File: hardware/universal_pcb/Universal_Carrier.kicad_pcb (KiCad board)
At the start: 2 copper layers, 100 x 70 mm, 98 parts

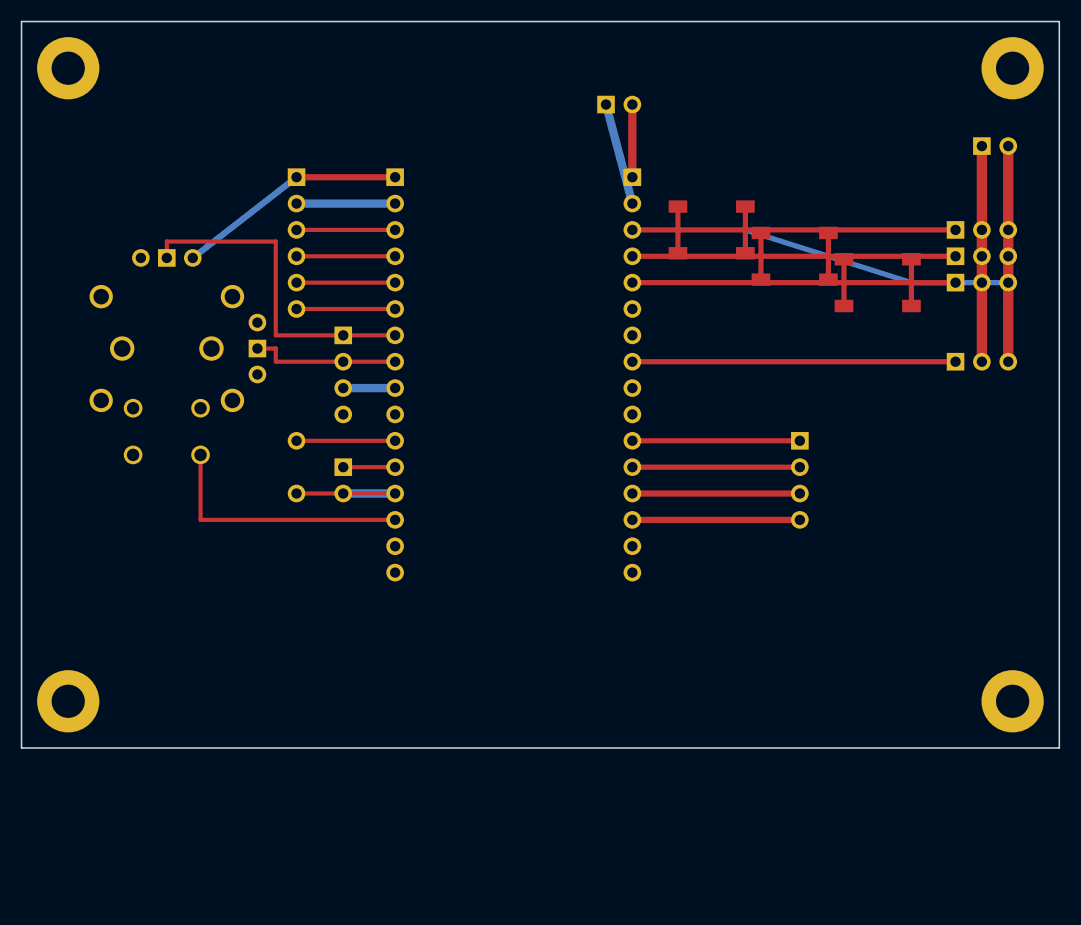
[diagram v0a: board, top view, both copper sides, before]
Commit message: chore: add local history tracking and lock files for universal pcb hardware project
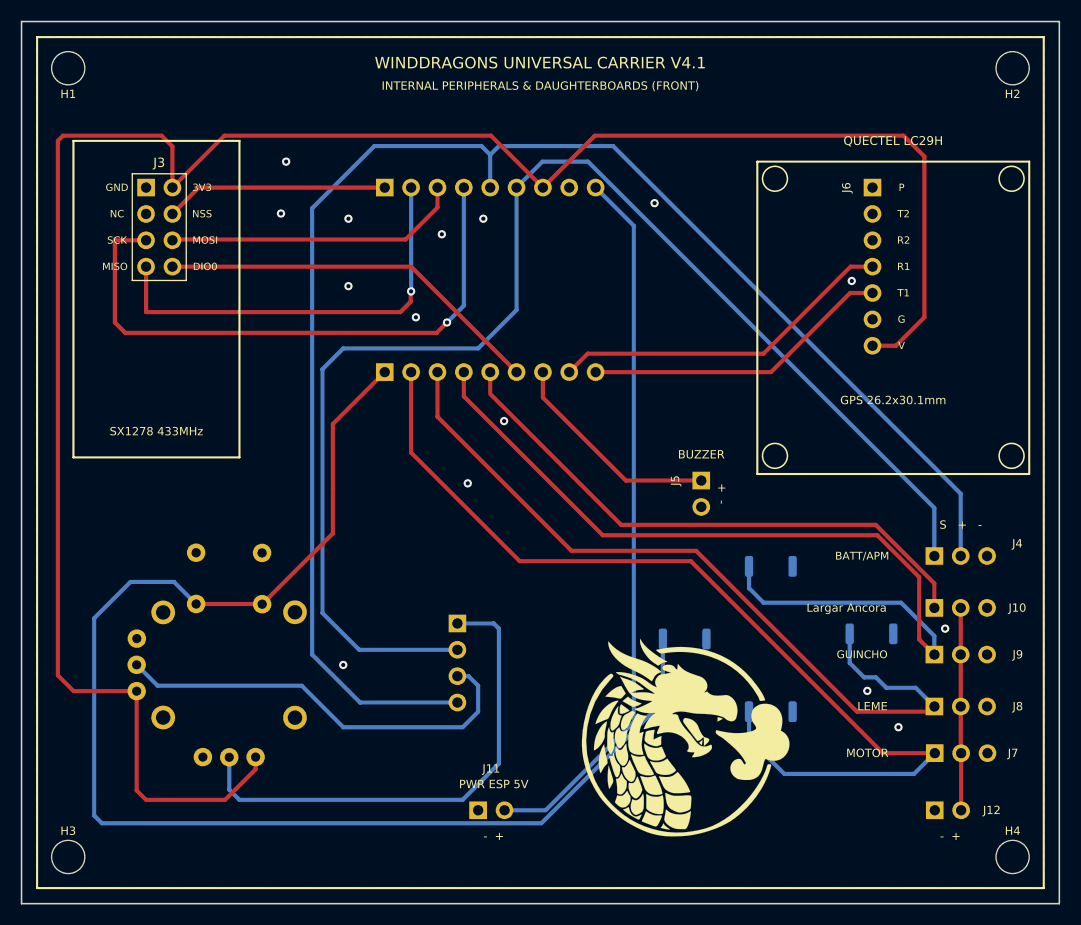
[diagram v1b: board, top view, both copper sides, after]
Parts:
- removed ? (x4): , MountingHole:MountingHole_3.2mm_M3_Pad
- removed ? (x82): , Connector_PinHeader_2.54mm:PinHeader_1x01_P2.54mm_Vertical
- removed ? (x12): , Button_Switch_SMD:SW_Push_1P1T_NO_6x6mm_H9.5mm
- added H1: MountingHole, MountingHole:MountingHole_3.2mm_M3, F.Cu at (4.50, 4.50)
- added H2: MountingHole, MountingHole:MountingHole_3.2mm_M3, F.Cu at (95.5, 4.50)
- added H3: MountingHole, MountingHole:MountingHole_3.2mm_M3, F.Cu at (4.50, 80.5)
- added H4: MountingHole, MountingHole:MountingHole_3.2mm_M3, F.Cu at (95.5, 80.5)
- added J1: ESP32_T_LANDSCAPE, Connector_PinHeader_2.54mm:PinHeader_1x09_P2.54mm_Horizontal, B.Cu at (35.0, 16.0)
- added J10: RACK_CREMALHEIRA, Connector_PinHeader_2.54mm:PinHeader_1x03_P2.54mm_Horizontal, F.Cu at (88.0, 56.5)
- added J11: PWR_ESP_5V, Connector_PinHeader_2.54mm:PinHeader_1x02_P2.54mm_Horizontal, F.Cu at (44.0, 76.0)
- added J12: PWR_SERVO_5V, Connector_PinHeader_2.54mm:PinHeader_1x02_P2.54mm_Horizontal, F.Cu at (88.0, 76.0)
- added J2: ESP32_B_LANDSCAPE, Connector_PinHeader_2.54mm:PinHeader_1x09_P2.54mm_Horizontal, B.Cu at (35.0, 33.8)
- added J3: SX1278_LORA_2x4, Connector_PinHeader_2.54mm:PinHeader_2x04_P2.54mm_Vertical, F.Cu at (12.0, 16.0)
- added J4: BATT_APM, Connector_PinHeader_2.54mm:PinHeader_1x03_P2.54mm_Horizontal, F.Cu at (88.0, 51.5)
- added J5: BUZZER, Connector_PinHeader_2.54mm:PinHeader_1x02_P2.54mm_Vertical, F.Cu at (65.5, 44.2)
- added J6: GPS_LC29H_7PIN, Connector_PinHeader_2.54mm:PinHeader_1x07_P2.54mm_Vertical, F.Cu at (82.0, 16.0)
- added J7: ESC_PROP_UP, Connector_PinHeader_2.54mm:PinHeader_1x03_P2.54mm_Horizontal, F.Cu at (88.0, 70.5)
- added J8: RUDDER_DN, Connector_PinHeader_2.54mm:PinHeader_1x03_P2.54mm_Horizontal, F.Cu at (88.0, 66.0)
- added J9: WINCH_MODE, Connector_PinHeader_2.54mm:PinHeader_1x03_P2.54mm_Horizontal, F.Cu at (88.0, 61.0)
- added JOY1: PS4_JOYSTICK, PS4_joystick:XDCR_COM-09032, B.Cu at (20.0, 62.0)
- added JP_RBL: REMOVE_BEFORE_LAUNCH, Connector_PinHeader_2.54mm:PinHeader_1x04_P2.54mm_Vertical, B.Cu at (42.0, 58.0)
- added LOGO1: WindDragons_Logo, WindDragons:WindDragons_Logo_20mm, F.Cu at (64.0, 69.0)
- added LOGO2: WindDragons_Logo, WindDragons:WindDragons_Logo_14mm, B.Cu at (50.5, 49.0)
- added SW1: UP, PS4_joystick:SKRKAEE020, B.Cu at (72.2, 66.5)
- added SW2: MODE, PS4_joystick:SKRKAEE020, B.Cu at (81.9, 59.0)
- added SW3: DOWN, PS4_joystick:SKRKAEE020, B.Cu at (72.2, 52.5)
- added SW4: BOOT, PS4_joystick:SKRKAEE020, B.Cu at (63.9, 59.5)
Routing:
- net 0: track 476.5 -> 0.00 mm
- net /+3V3: track 0.00 -> 200.3 mm
- net /IO1_ADC: track 0.00 -> 147.6 mm
- net /IO9_BOOT: track 0.00 -> 130.8 mm
- net /IO0_ADC: track 0.00 -> 130.6 mm
- net /IO18_ACT1_UP: track 0.00 -> 93.0 mm
- net /IO20_RUDDER_DN: track 0.00 -> 85.2 mm
- net /IO19_WINCH_MODE: track 0.00 -> 77.3 mm
- net /+5V: track 0.00 -> 69.0 mm
- net /IO2_SCK: track 0.00 -> 57.5 mm, vias 0 -> 1
- net /IO23_ACT4: track 0.00 -> 55.3 mm
- net /JOY_X: track 0.00 -> 48.2 mm
- net /JOY_Y: track 0.00 -> 41.6 mm
- net /IO4_MISO: track 0.00 -> 41.3 mm, vias 0 -> 1
- net /IO12_LORA_DIO0: track 0.00 -> 37.4 mm
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- added copper zone on B.Cu, net /GND
- added copper zone on F.Cu, net /GND
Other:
- board size 100 x 70 mm -> 100 x 85 mm
- rule pad_to_mask_clearance: 0.1 -> 0.05
- board text added: "+ -"
- board text added: "- +"
- board text added: "BATT/APM"
- board text added: "BUZZER"
- board text added: "GPS 26.2x30.1mm"
- board text added: "GUINCHO"
- board text added: "INTERNAL PERIPHERALS & DAUGHTERBOARDS (FRONT)"
- board text added: "LEME"
- board text added: "Largar Ancora"
- board text added: "MOTOR"
- board text added: "PS4 3D JOYSTICK"
- board text added: "PWR ESP 5V"
- board text added: "QUECTEL LC29H"
- board text added: "REMOVE BEFORE LAUNCH"
- board text added: "S + -"
- board text added: "SOLID GND COPPER PLANES ON F.CU & B.CU (100x85mm)"
- board text added: "ST7789 1.47 INCH LCD (320x172)"
- board text added: "SX1278 433MHz"
- board text added: "USB-C"
- board text added: "USER INTERFACE: DISPLAY & PS4 JOYSTICK"
- board text added: "WINDDRAGONS REMOTE CONTROL & CARRIER V4.1"
- board text added: "WINDDRAGONS UNIVERSAL CARRIER V4.1"
- board text added: "X: 1-2 | Y: 3-4"

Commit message: feat: add new universal PCB gerbers, logos, and updated design files
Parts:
- moved LOGO1 4.12 mm to (60.0, 68.0)
- moved LOGO2 1.00 mm to (50.5, 48.0)

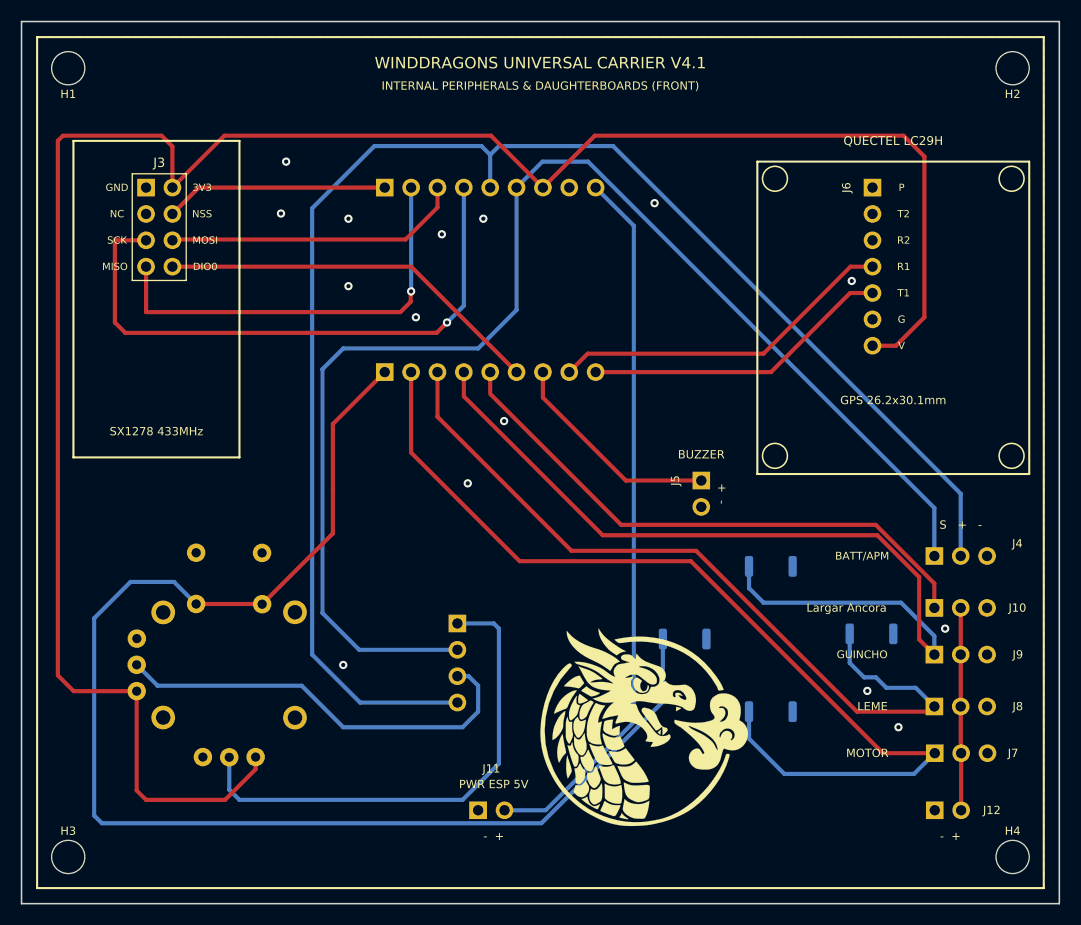
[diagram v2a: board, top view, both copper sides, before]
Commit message: feat: update PCB gerber files and add logo bitmap header
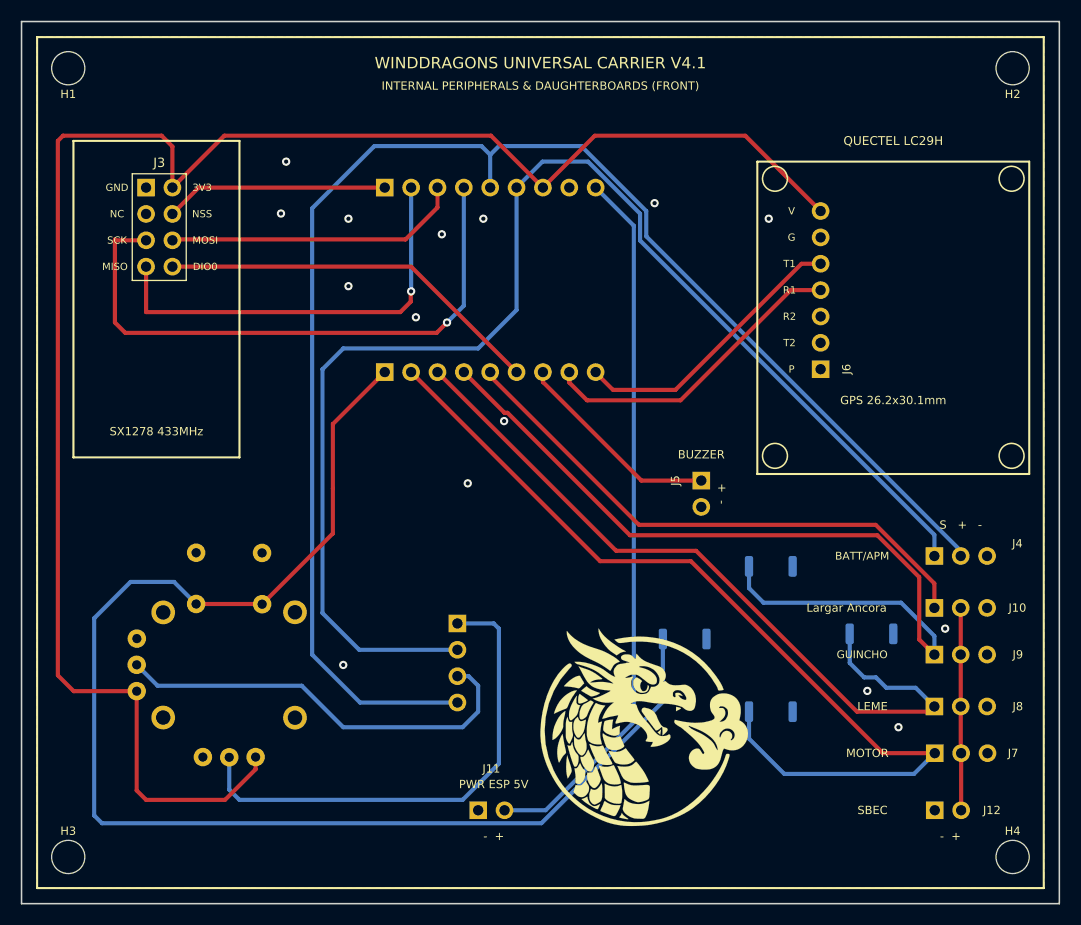
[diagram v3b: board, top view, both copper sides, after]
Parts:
- moved J6 18.2 mm to (77.0, 33.5), turned to 180 degrees
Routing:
- net /+3V3: track 200.3 -> 170.8 mm
- net /IO18_ACT1_UP: track 93.0 -> 88.5 mm
- net /IO16_GPS_RX: track 33.4 -> 30.3 mm
- net /IO19_WINCH_MODE: track 77.3 -> 74.8 mm
- net /IO17_GPS_TX: track 29.8 -> 27.5 mm
- net /IO1_ADC: track 147.6 -> 145.8 mm
- net /IO20_RUDDER_DN: track 85.2 -> 83.8 mm
- net /IO13_BUZ: track 21.0 -> 20.2 mm
- net /IO23_ACT4: track 55.3 -> 54.5 mm
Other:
- board text added: "SBEC"

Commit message: feat: add web configuration page and API endpoints for screen brightness control and system settings
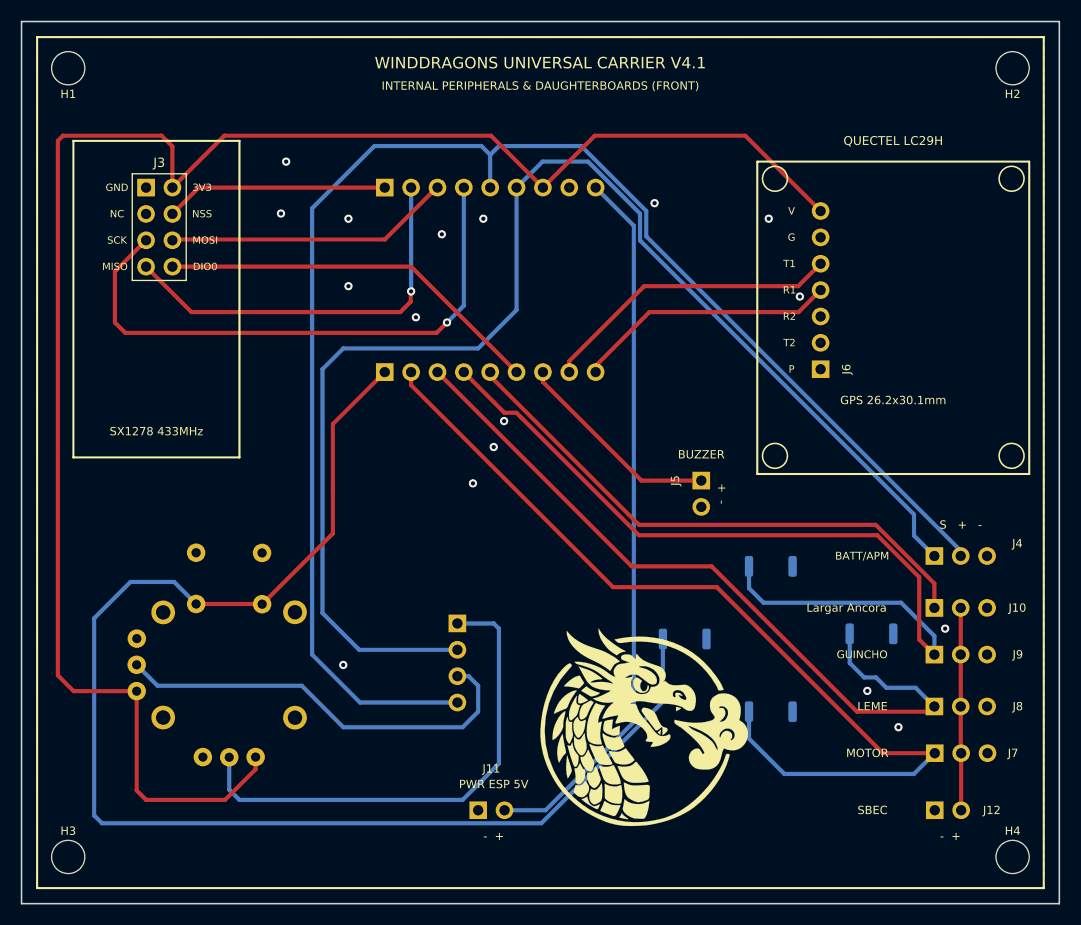
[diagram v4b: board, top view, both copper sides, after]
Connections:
- J6 pad 4: /IO16_GPS_RX -> /IO17_GPS_TX
- J6 pad 5: /IO17_GPS_TX -> /IO16_GPS_RX
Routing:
- net /IO4_MISO: track 41.3 -> 38.7 mm
- net /IO17_GPS_TX: track 27.5 -> 25.3 mm
- net /IO2_SCK: track 57.5 -> 55.7 mm
- net /IO16_GPS_RX: track 30.3 -> 29.2 mm
- net /IO3_MOSI: track 28.8 -> 27.6 mm
- net /IO18_ACT1_UP: track 88.5 -> 89.2 mm
- net /GND: vias 15 -> 17

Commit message: feat: add hardware joystick testing page and update universal carrier PCB and gerber files
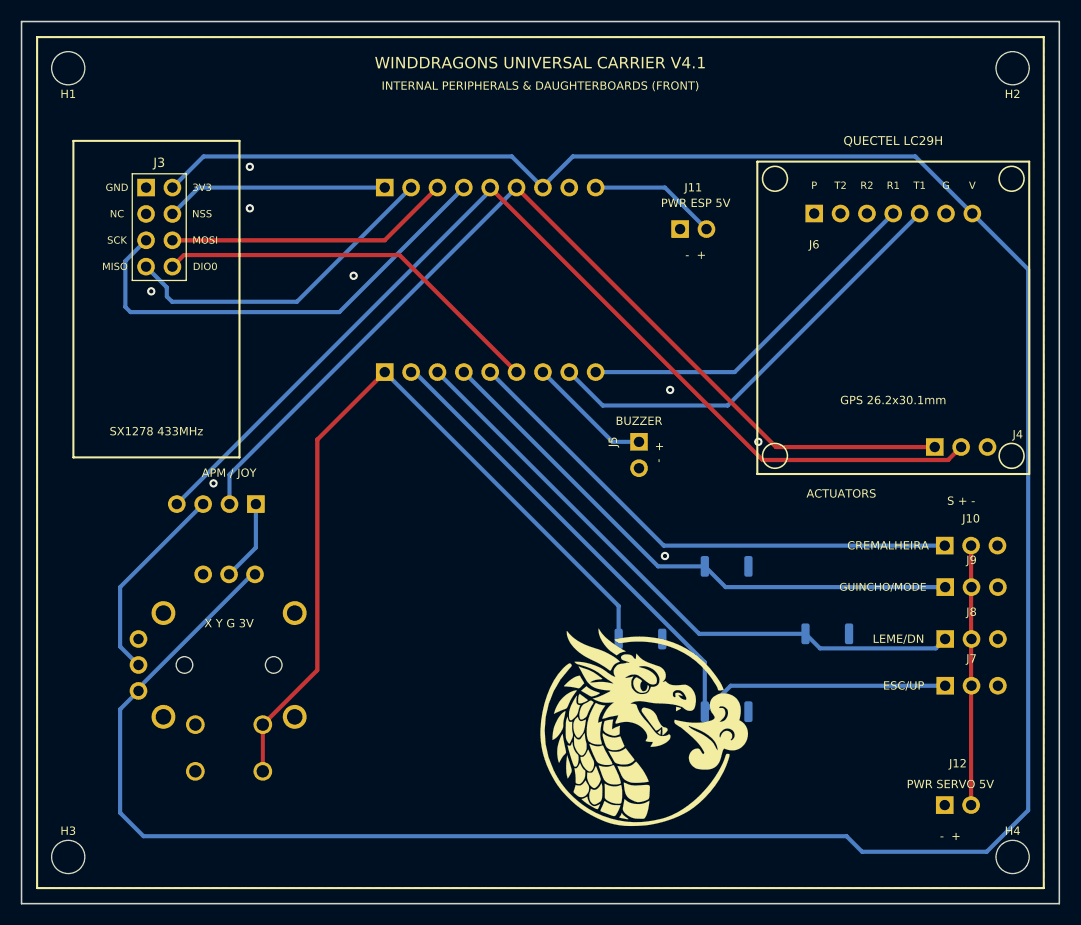
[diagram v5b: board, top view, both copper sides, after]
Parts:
- J6: footprint Connector_PinHeader_2.54mm:PinHeader_1x07_P2.54mm_Vertical -> Connector_PinHeader_2.54mm:PinHeader_1x07_P2.54mm_Horizontal
- JOY1: value PS4_JOYSTICK -> PS5_JOYSTICK; footprint PS4_joystick:XDCR_COM-09032 -> PS5_joystick:Alps_RKJXV1224005
- moved J11 59.3 mm to (63.5, 20.0)
- moved JP_RBL 22.6 mm to (22.6, 46.5), turned to -90 degrees
- moved J6 15.0 mm to (76.4, 18.5), turned to 0 degrees
- moved LOGO2 10.9 mm to (40.0, 51.0)
- moved J4 10.5 mm to (88.0, 41.0)
- moved J5 7.06 mm to (59.5, 40.5)
- moved J8 6.58 mm to (89.0, 59.5)
- moved J9 6.58 mm to (89.0, 54.5)
- moved J7 6.58 mm to (89.0, 64.0)
- moved J10 6.08 mm to (89.0, 50.5)
- moved SW1 4.26 mm to (67.9, 66.5)
- moved SW2 4.26 mm to (77.6, 59.0)
- moved SW3 4.26 mm to (67.9, 52.5)
- moved SW4 4.26 mm to (59.6, 59.5)
- moved J12 1.08 mm to (89.0, 75.5)
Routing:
- net /+3V3: track 170.8 -> 262.1 mm
- net /+5V: track 69.0 -> 12.3 mm
- net /IO9_BOOT: track 130.8 -> 78.4 mm
- net /IO1_ADC: track 145.8 -> 99.8 mm
- net /JOY_X: track 48.2 -> 7.84 mm
- net /IO0_ADC: track 130.6 -> 92.6 mm
- net /IO20_RUDDER_DN: track 83.8 -> 55.0 mm
- net /JOY_Y: track 41.6 -> 19.5 mm
- net /IO18_ACT1_UP: track 89.2 -> 68.8 mm
- net /IO19_WINCH_MODE: track 74.8 -> 60.3 mm
- net /IO16_GPS_RX: track 29.2 -> 42.8 mm
- net /IO2_SCK: track 55.7 -> 45.0 mm, vias 1 -> 0
- net /IO17_GPS_TX: track 25.3 -> 35.0 mm
- net /IO13_BUZ: track 20.2 -> 12.0 mm
- net /IO4_MISO: track 38.7 -> 32.0 mm, vias 1 -> 0
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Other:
- board text added: "ACTUATORS"
- board text added: "APM / JOY"
- board text added: "CREMALHEIRA"
- board text added: "ESC/UP"
- board text added: "GUINCHO/MODE"
- board text added: "LEME/DN"
- board text added: "PS5 3D JOYSTICK (ALPS RKJXV)"
- board text added: "PWR SERVO 5V"
- board text added: "USER INTERFACE: DISPLAY & PS5 JOYSTICK"
- board text added: "X Y G 3V"
- board text removed: "BATT/APM"
- board text removed: "GUINCHO"
- board text removed: "LEME"
- board text removed: "Largar Ancora"
- board text removed: "MOTOR"
- board text removed: "PS4 3D JOYSTICK"
- board text removed: "REMOVE BEFORE LAUNCH"
- board text removed: "SBEC"
- board text removed: "USER INTERFACE: DISPLAY & PS4 JOYSTICK"
- board text removed: "X: 1-2 | Y: 3-4"

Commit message: update universal carrier PCB layout, gerber files, and rover control interface
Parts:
- removed LOGO2: WindDragons_Logo, WindDragons:WindDragons_Logo_14mm
- added LOGO1: WindDragons_Logo, WindDragons:WindDragons_Logo_20mm, B.Cu at (43.5, 50.0)
- moved LOGO1 12.1 mm to (50.5, 60.5)
- moved J4 9.86 mm to (79.5, 46.0)
- moved J3 4.00 mm to (12.0, 20.0)
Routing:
- net /IO1_ADC: track 99.8 -> 94.0 mm
- net /IO0_ADC: track 92.6 -> 86.9 mm
- net /IO2_SCK: track 45.0 -> 47.6 mm
- net /IO12_LORA_DIO0: track 38.3 -> 36.5 mm
- net /IO4_MISO: track 32.0 -> 33.7 mm
- net /IO3_MOSI: track 27.6 -> 29.3 mm
- net /IO5_NSS: track 21.5 -> 22.9 mm
- net /GND: vias 8 -> 6
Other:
- board text added: "(FRONT)"
- board text added: "TELEMETRIA BAT."
- board text added: "WINDDRAGONS VIRTUAL REGATTA V4.1"
- board text added: "detector ancora"
- board text removed: "ACTUATORS"
- board text removed: "BUZZER"
- board text removed: "INTERNAL PERIPHERALS & DAUGHTERBOARDS (FRONT)"
- board text removed: "WINDDRAGONS REMOTE CONTROL & CARRIER V4.1"
- board text removed: "WINDDRAGONS UNIVERSAL CARRIER V4.1"
